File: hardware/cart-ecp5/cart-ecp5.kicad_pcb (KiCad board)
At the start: 4 copper layers, 100 x 60 mm, 129 parts, among them J1 JTAG, J2 MicroSD_Molex_1040310811, J3 N64_Cartridge_Bus, J5 USB_C_USB2.0, U1 LFE5U-25F-xBG256x, U10 93C46BT-I_OT, U11 FT2232HQ, U13 TLV62568DBV, U2 W25Q512JVEIM, U3 S27KS0641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

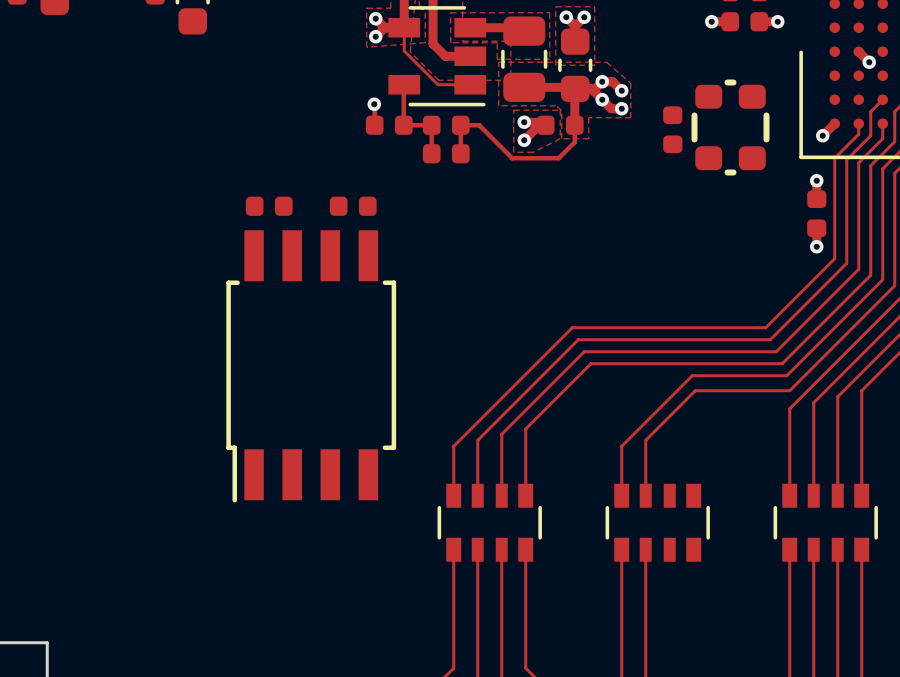
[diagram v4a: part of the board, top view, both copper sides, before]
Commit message: Route the N64 CIC emulation interface
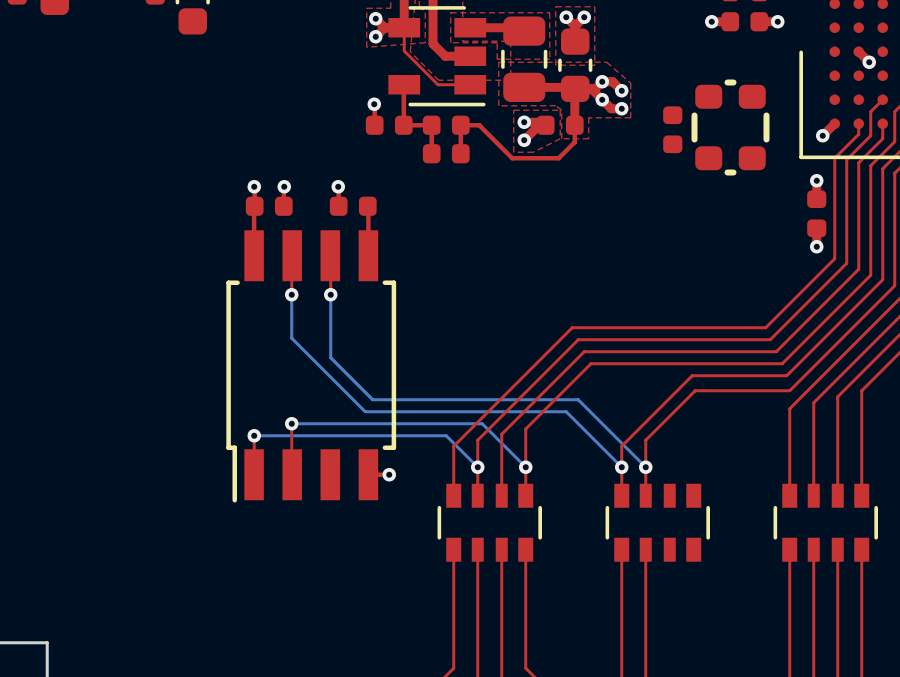
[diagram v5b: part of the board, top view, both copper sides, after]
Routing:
- net N64_CIC_DATA1: track 18.2 -> 33.7 mm, vias 0 -> 2
- net N64_CIC_DATA2: track 19.0 -> 34.4 mm, vias 0 -> 2
- net N64_S_CLK: track 22.2 -> 32.3 mm, vias 0 -> 2
- net N64_COLD_RESET#: track 22.5 -> 31.7 mm, vias 0 -> 2
- net P3V3: track 64.2 -> 66.6 mm, vias 41 -> 42
- net GND: track 181.7 -> 183.7 mm, vias 105 -> 108
- net Net-(R6-Pad2): track 0.00 -> 1.66 mm
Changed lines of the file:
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@@
     (thickness 1.2)
     (drawings 36)
-    (tracks 1317)
+    (tracks 1364)
     (zones 0)
     (modules 129)
@@
   (segment (start 115.524999 102.025001) (end 115.524999 101.325) (width 0.15) (layer F.Cu) (net 1))
   (segment (start 115.05 102.5) (end 115.524999 102.025001) (width 0.15) (layer F.Cu) (net 1))
+  (via (at 127.45 108.3) (size 0.45) (drill 0.2) (layers F.Cu B.Cu) (net 1))
+  (segment (start 127.465 108.315) (end 127.45 108.3) (width 0.15) (layer F.Cu) (net 1))
+  (segment (start 127.465 108.95) (end 127.465 108.315) (width 0.15) (layer F.Cu) (net 1))
+  (via (at 125.65 108.3) (size 0.45) (drill 0.2) (layers F.Cu B.Cu) (net 1))
+  (segment (start 125.635 108.315) (end 125.65 108.3) (width 0.15) (layer F.Cu) (net 1))
+  (segment (start 125.635 108.95) (end 125.635 108.315) (width 0.15) (layer F.Cu) (net 1))
+  (via (at 129.15 117.9) (size 0.45) (drill 0.2) (layers F.Cu B.Cu) (net 1))
+  (segment (start 128.455 117.9) (end 129.15 117.9) (width 0.15) (layer F.Cu) (net 1))
   (via (at 128.7 103.299994) (size 0.45) (drill 0.2) (layers F.Cu B.Cu) (net 2))
   (via (at 128.699976 102.7) (size 0.45) (drill 0.2) (layers F.Cu B.Cu) (net 2))
@@
   (segment (start 113.465 101.335) (end 113.475 101.325) (width 0.15) (layer F.Cu) (net 2))
   (segment (start 113.465 102.5) (end 113.465 101.335) (width 0.15) (layer F.Cu) (net 2))
+  (segment (start 124.645 108.97) (end 124.665 108.95) (width 0.15) (layer F.Cu) (net 2))
+  (segment (start 124.645 110.6) (end 124.645 108.97) (width 0.15) (layer F.Cu) (net 2))
+  (segment (start 124.665 108.315) (end 124.65 108.3) (width 0.15) (layer F.Cu) (net 2))
+  (via (at 124.65 108.3) (size 0.45) (drill 0.2) (layers F.Cu B.Cu) (net 2))
+  (segment (start 124.665 108.95) (end 124.665 108.315) (width 0.15) (layer F.Cu) (net 2))
   (segment (start 160.3 116) (end 160.3 118.6) (width 0.1) (layer F.Cu) (net 3))
   (segment (start 151.6 107.3) (end 160.3 116) (width 0.1) (layer F.Cu) (net 3))
@@
   (segment (start 141.85 113.4) (end 144.4 110.85) (width 0.1) (layer F.Cu) (net 16))
   (segment (start 135.45 113.4) (end 141.85 113.4) (width 0.1) (layer F.Cu) (net 16))
-  (segment (start 132.1 118.6) (end 132.1 116.75) (width 0.1) (layer F.Cu) (net 16))
+  (segment (start 132.1 118.6) (end 132.1 117.65) (width 0.1) (layer F.Cu) (net 16))
   (segment (start 132.1 116.75) (end 135.45 113.4) (width 0.1) (layer F.Cu) (net 16))
   (segment (start 145.2 105.8) (end 145.6 105.4) (width 0.1) (layer F.Cu) (net 16))
   (segment (start 144.4 107.4) (end 145.2 106.6) (width 0.1) (layer F.Cu) (net 16))
   (segment (start 144.4 110.85) (end 144.4 107.4) (width 0.1) (layer F.Cu) (net 16))
+  (segment (start 132.1 117.65) (end 132.1 116.75) (width 0.1) (layer F.Cu) (net 16))
+  (via (at 132.1 117.65) (size 0.45) (drill 0.2) (layers F.Cu B.Cu) (net 16))
+  (via (at 124.65 116.6) (size 0.45) (drill 0.2) (layers F.Cu B.Cu) (net 16))
+  (segment (start 131.05 116.6) (end 124.65 116.6) (width 0.1) (layer B.Cu) (net 16))
+  (segment (start 132.1 117.65) (end 131.05 116.6) (width 0.1) (layer B.Cu) (net 16))
+  (segment (start 124.65 117.895) (end 124.645 117.9) (width 0.1) (layer F.Cu) (net 16))
+  (segment (start 124.65 116.6) (end 124.65 117.895) (width 0.1) (layer F.Cu) (net 16))
   (segment (start 146 106.8) (end 146 105.8) (width 0.1) (layer F.Cu) (net 17))
   (segment (start 145.2 107.6) (end 146 106.8) (width 0.1) (layer F.Cu) (net 17))
@@
   (segment (start 142.25 114.2) (end 145.2 111.25) (width 0.1) (layer F.Cu) (net 17))
   (segment (start 146 105.8) (end 146.4 105.4) (width 0.1) (layer F.Cu) (net 17))
-  (segment (start 133.7 118.6) (end 133.7 116.375) (width 0.1) (layer F.Cu) (net 17))
+  (segment (start 133.7 118.6) (end 133.7 117.65) (width 0.1) (layer F.Cu) (net 17))
   (segment (start 135.875 114.2) (end 142.25 114.2) (width 0.1) (layer F.Cu) (net 17))
   (segment (start 133.7 116.375) (end 135.875 114.2) (width 0.1) (layer F.Cu) (net 17))
+  (segment (start 133.7 117.65) (end 133.7 116.375) (width 0.1) (layer F.Cu) (net 17))
+  (via (at 133.7 117.65) (size 0.45) (drill 0.2) (layers F.Cu B.Cu) (net 17))
+  (via (at 125.9 116.2) (size 0.45) (drill 0.2) (layers F.Cu B.Cu) (net 17))
+  (segment (start 132.25 116.2) (end 125.9 116.2) (width 0.1) (layer B.Cu) (net 17))
+  (segment (start 133.7 117.65) (end 132.25 116.2) (width 0.1) (layer B.Cu) (net 17))
+  (segment (start 125.9 117.885) (end 125.915 117.9) (width 0.1) (layer F.Cu) (net 17))
+  (segment (start 125.9 116.2) (end 125.9 117.885) (width 0.1) (layer F.Cu) (net 17))
   (segment (start 144 107.35) (end 144.8 106.55) (width 0.1) (layer F.Cu) (net 18))
   (segment (start 144.8 106.55) (end 144.8 106.2) (width 0.1) (layer F.Cu) (net 18))
@@
   (segment (start 147.05 88.6) (end 147.05 88.6) (width 0.1) (layer B.Cu) (net 168))
   (via (at 147.05 88.6) (size 0.45) (drill 0.2) (layers F.Cu B.Cu) (net 168))
-  (segment (start 142.85 83.85) (end 147.05 88.05) (width 0.1) (layer F.Cu) (net 168))
-  (segment (start 136.2 83.85) (end 142.85 83.85) (width 0.1) (layer F.Cu) (net 168))
+  (segment (start 133.95 84.44) (end 135.61 84.44) (width 0.1) (layer F.Cu) (net 168))
   (segment (start 135.61 84.44) (end 136.2 83.85) (width 0.1) (layer F.Cu) (net 168))
+  (segment (start 136.2 83.85) (end 142.85 83.85) (width 0.1) (layer F.Cu) (net 168))
   (segment (start 147.05 88.05) (end 147.05 88.6) (width 0.1) (layer F.Cu) (net 168))
-  (segment (start 133.95 84.44) (end 135.61 84.44) (width 0.1) (layer F.Cu) (net 168))
+  (segment (start 142.85 83.85) (end 147.05 88.05) (width 0.1) (layer F.Cu) (net 168))
   (segment (start 147.6 87.95) (end 142.82 83.17) (width 0.1) (layer F.Cu) (net 169))
   (segment (start 142.82 83.17) (end 142.63 83.17) (width 0.1) (layer F.Cu) (net 169))
@@
   (segment (start 133.7 124.35) (end 133.7 120.4) (width 0.1) (layer F.Cu) (net 282))
   (segment (start 135 125.65) (end 133.7 124.35) (width 0.1) (layer F.Cu) (net 282))
+  (segment (start 128.455 108.97) (end 128.435 108.95) (width 0.15) (layer F.Cu) (net 283))
+  (segment (start 128.455 110.6) (end 128.455 108.97) (width 0.15) (layer F.Cu) (net 283))
   (segment (start 169.1 103.8) (end 168.3 104.6) (width 0.1) (layer F.Cu) (net 284))
   (segment (start 169.1 100) (end 169.1 103.8) (width 0.1) (layer F.Cu) (net 284))
@@
   (segment (start 136.9 125.6) (end 136.9 125.65) (width 0.1) (layer F.Cu) (net 292))
   (segment (start 137.5 126.25) (end 136.9 125.65) (width 0.1) (layer B.Cu) (net 292))
-  (segment (start 136.9 116.95) (end 136.9 118.6) (width 0.1) (layer F.Cu) (net 295))
+  (segment (start 136.9 116.95) (end 136.9 117.65) (width 0.1) (layer F.Cu) (net 295))
   (segment (start 139.25 114.6) (end 136.9 116.95) (width 0.1) (layer F.Cu) (net 295))
   (segment (start 145.6 107.7) (end 145.6 111.4) (width 0.1) (layer F.Cu) (net 295))
@@
   (segment (start 145.6 111.4) (end 142.4 114.6) (width 0.1) (layer F.Cu) (net 295))
   (segment (start 146.4 106.9) (end 145.6 107.7) (width 0.1) (layer F.Cu) (net 295))
-  (segment (start 137.7 116.75) (end 137.7 118.6) (width 0.1) (layer F.Cu) (net 296))
+  (segment (start 136.9 117.65) (end 136.9 118.6) (width 0.1) (layer F.Cu) (net 295))
+  (via (at 136.9 117.65) (size 0.45) (drill 0.2) (layers F.Cu B.Cu) (net 295))
+  (via (at 125.9 111.9) (size 0.45) (drill 0.2) (layers F.Cu B.Cu) (net 295))
+  (segment (start 125.9 110.615) (end 125.915 110.6) (width 0.1) (layer F.Cu) (net 295))
+  (segment (start 125.9 111.9) (end 125.9 110.615) (width 0.1) (layer F.Cu) (net 295))
+  (segment (start 125.9 113.35) (end 125.9 111.9) (width 0.1) (layer B.Cu) (net 295))
+  (segment (start 128.35 115.8) (end 125.9 113.35) (width 0.1) (layer B.Cu) (net 295))
+  (segment (start 135.05 115.8) (end 128.35 115.8) (width 0.1) (layer B.Cu) (net 295))
+  (segment (start 136.9 117.65) (end 135.05 115.8) (width 0.1) (layer B.Cu) (net 295))
+  (segment (start 137.7 116.75) (end 137.7 117.65) (width 0.1) (layer F.Cu) (net 296))
   (segment (start 139.35 115.1) (end 137.7 116.75) (width 0.1) (layer F.Cu) (net 296))
   (segment (start 142.5 115.1) (end 139.35 115.1) (width 0.1) (layer F.Cu) (net 296))
@@
   (segment (start 146.8 105.8) (end 146.8 107.05) (width 0.1) (layer F.Cu) (net 296))
   (segment (start 147.2 105.4) (end 146.8 105.8) (width 0.1) (layer F.Cu) (net 296))
+  (segment (start 137.7 117.65) (end 137.7 118.6) (width 0.1) (layer F.Cu) (net 296))
+  (via (at 137.7 117.65) (size 0.45) (drill 0.2) (layers F.Cu B.Cu) (net 296))
+  (via (at 127.2 111.9) (size 0.45) (drill 0.2) (layers F.Cu B.Cu) (net 296))
+  (segment (start 127.2 110.615) (end 127.185 110.6) (width 0.1) (layer F.Cu) (net 296))
+  (segment (start 127.2 111.9) (end 127.2 110.615) (width 0.1) (layer F.Cu) (net 296))
+  (segment (start 128.6 115.4) (end 127.2 114) (width 0.1) (layer B.Cu) (net 296))
+  (segment (start 127.2 114) (end 127.2 111.9) (width 0.1) (layer B.Cu) (net 296))
+  (segment (start 135.45 115.4) (end 128.6 115.4) (width 0.1) (layer B.Cu) (net 296))
+  (segment (start 137.7 117.65) (end 135.45 115.4) (width 0.1) (layer B.Cu) (net 296))
   (segment (start 104.235 82.025) (end 105.165 82.025) (width 0.15) (layer F.Cu) (net 299))
   (segment (start 105.165 82.025) (end 105.165 82.975) (width 0.15) (layer F.Cu) (net 299))

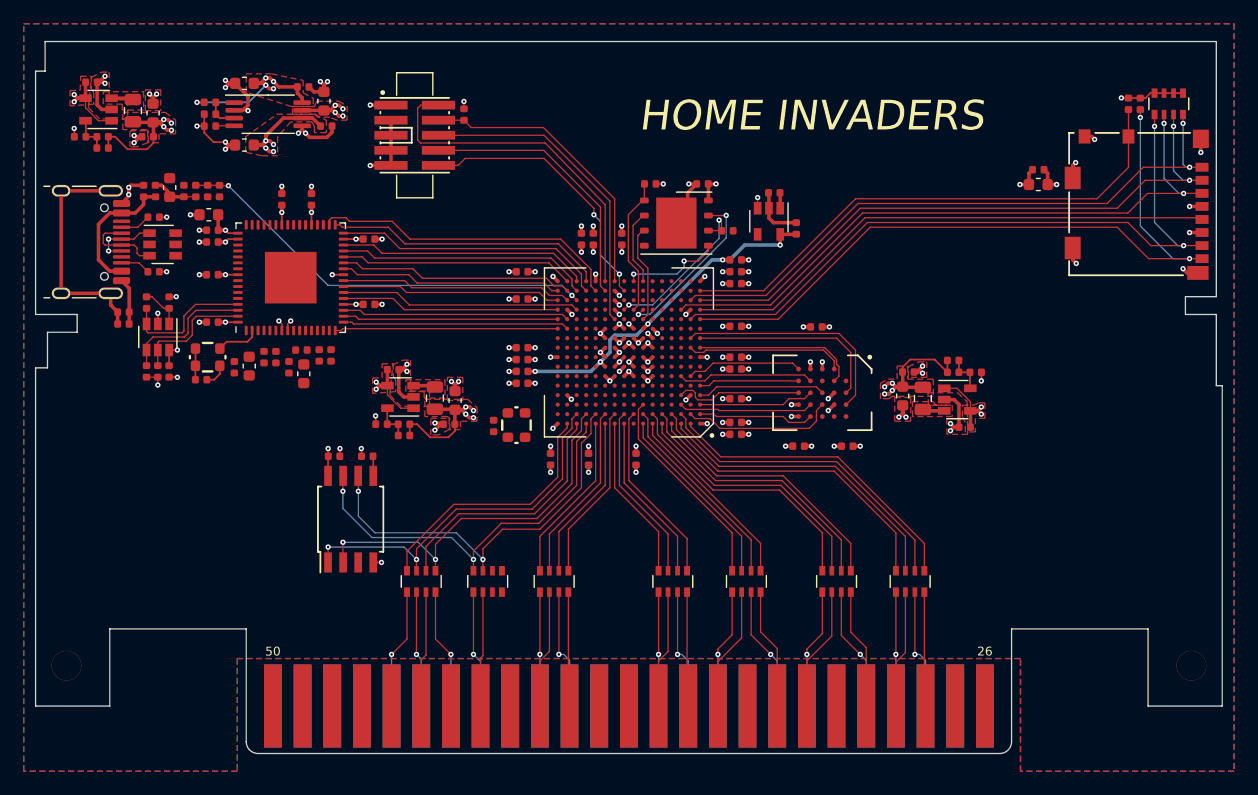
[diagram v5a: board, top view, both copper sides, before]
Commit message: Tighten up switcher placement to gauge available space
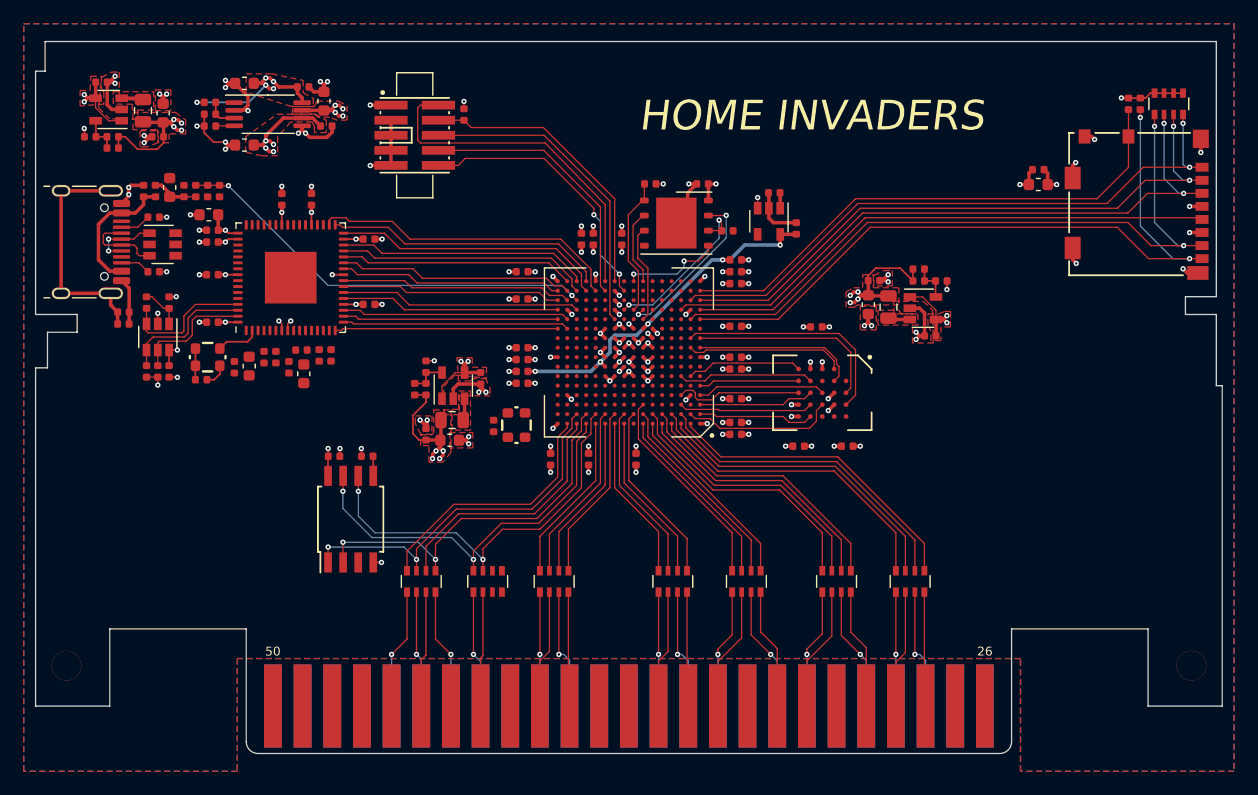
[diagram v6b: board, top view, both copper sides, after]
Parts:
- moved C65 8.23 mm to (175.4, 98.8)
- moved L3 8.23 mm to (171.9, 96.4)
- moved R31 8.23 mm to (176.3, 94.2)
- moved U13 8.23 mm to (174.8, 96.5)
- moved C66 8.23 mm to (174.4, 93.2)
- moved C67 8.23 mm to (170.2, 96.2)
- moved R30 8.23 mm to (174.4, 94.2)
- moved C68 8.23 mm to (170.7, 94.2)
- moved C11 7.41 mm to (137.5, 102.4), turned to 270 degrees
- moved R13 6.13 mm to (132.9, 101.4), turned to 90 degrees
- moved U7 4.55 mm to (135.2, 103.0), turned to 90 degrees
- moved C15 4.00 mm to (131.9, 103.3), turned to 90 degrees
- moved R12 3.48 mm to (132.9, 103.3), turned to 90 degrees
- moved C17 3.38 mm to (134.9, 107.6), turned to 0 degrees
- moved L2 2.35 mm to (135.1, 105.9), turned to 180 degrees
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
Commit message: Adjust trace widths and spacings for impedance control
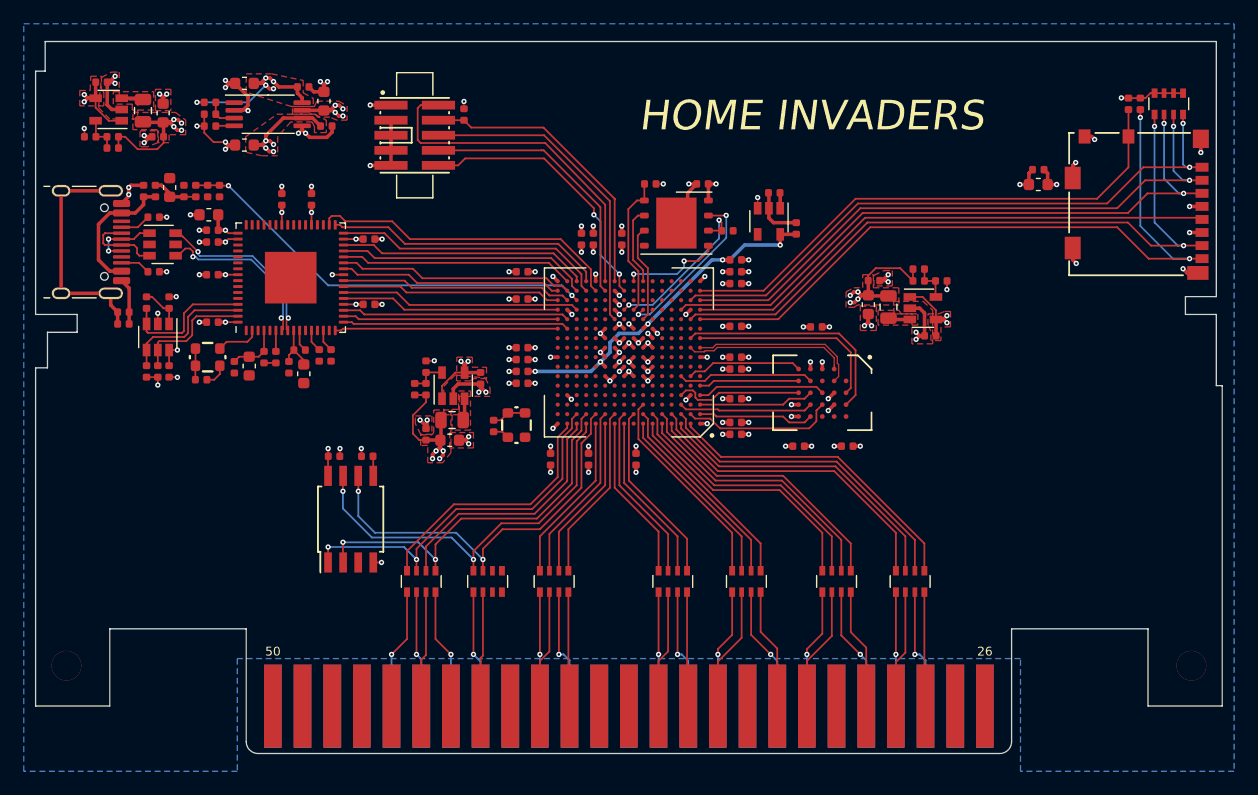
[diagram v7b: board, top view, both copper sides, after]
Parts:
- moved C24 0.15 mm to (122.2, 100.0)
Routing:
- net /Interface-USB/USB_D+: track 0.90 -> 15.0 mm, vias 1 -> 2
- net /Interface-USB/USB_D-: track 0.90 -> 14.5 mm, vias 1 -> 2
- net /Interface-USB/USB_VPHY: track 0.00 -> 4.62 mm
- net /Interface-USB/USB_VPLL: track 0.00 -> 4.35 mm
- net GND: track 183.7 -> 187.9 mm
- net P3V3: track 66.6 -> 69.5 mm
- net Net-(R21-Pad1): track 0.00 -> 1.88 mm
- net /Interface-USB/USB_1V8: track 6.40 -> 8.28 mm
- net Net-(R22-Pad1): track 0.00 -> 1.77 mm
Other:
- net class Default: trace_width 0.1 -> 0.15
- net class HRAM_CK added: clearance 0.1, trace_width 0.11, via_dia 0.45, via_drill 0.2
- net class USB_D added: clearance 0.1, trace_width 0.14, via_dia 0.45, via_drill 0.2

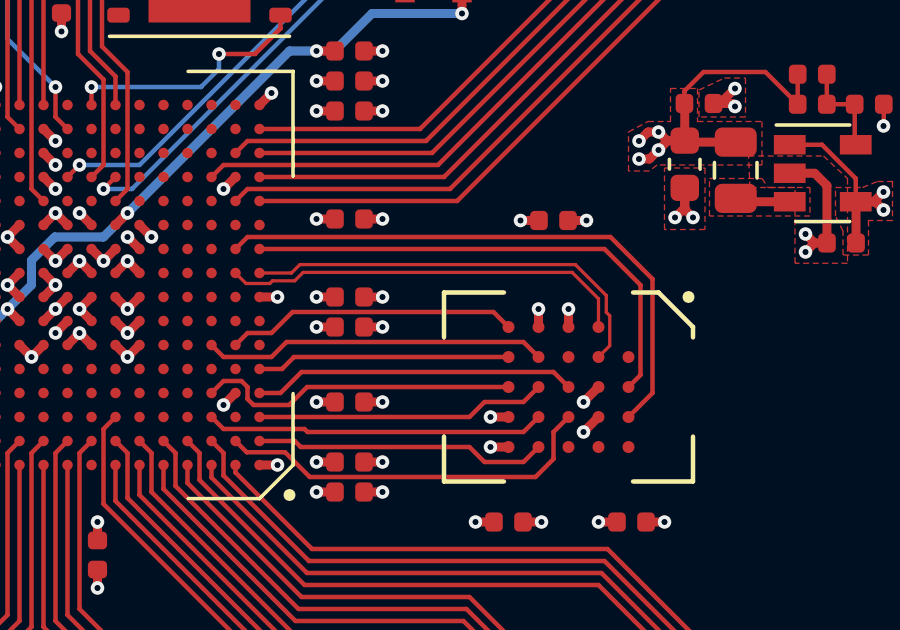
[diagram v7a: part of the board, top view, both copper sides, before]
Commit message: Glosses before length matching HRAM_DQx and HRAM_RDQS
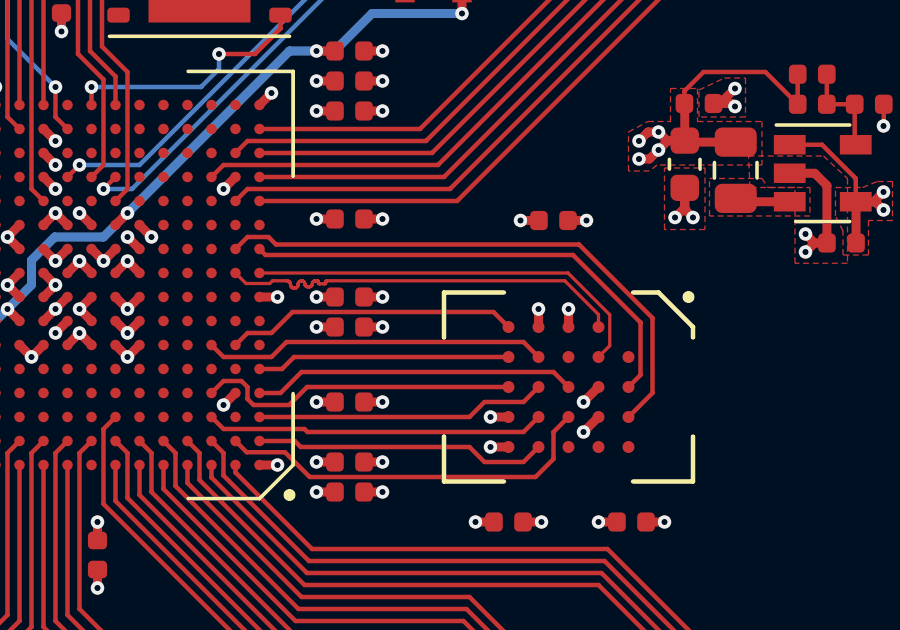
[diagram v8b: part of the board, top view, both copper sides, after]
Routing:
- net HRAM_RESET_B: track 19.6 -> 18.8 mm
- net HRAM_CS_B: track 16.8 -> 16.0 mm
- net HRAM_CK_P: track 14.4 -> 13.8 mm
